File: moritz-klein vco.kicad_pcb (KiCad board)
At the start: 2 copper layers, 150 x 100 mm, 92 parts, among them J1 AudioJack2_SwitchT, J10 AudioJack2_SwitchT, J11 AudioJack2_SwitchT, J12 AudioJack2_SwitchT, J13 Conn_02x05_Odd_Even, J2 AudioJack2_SwitchT, J3 AudioJack2_SwitchT, J4 AudioJack2_SwitchT, J5 AudioJack2_SwitchT, J6 AudioJack2_SwitchT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

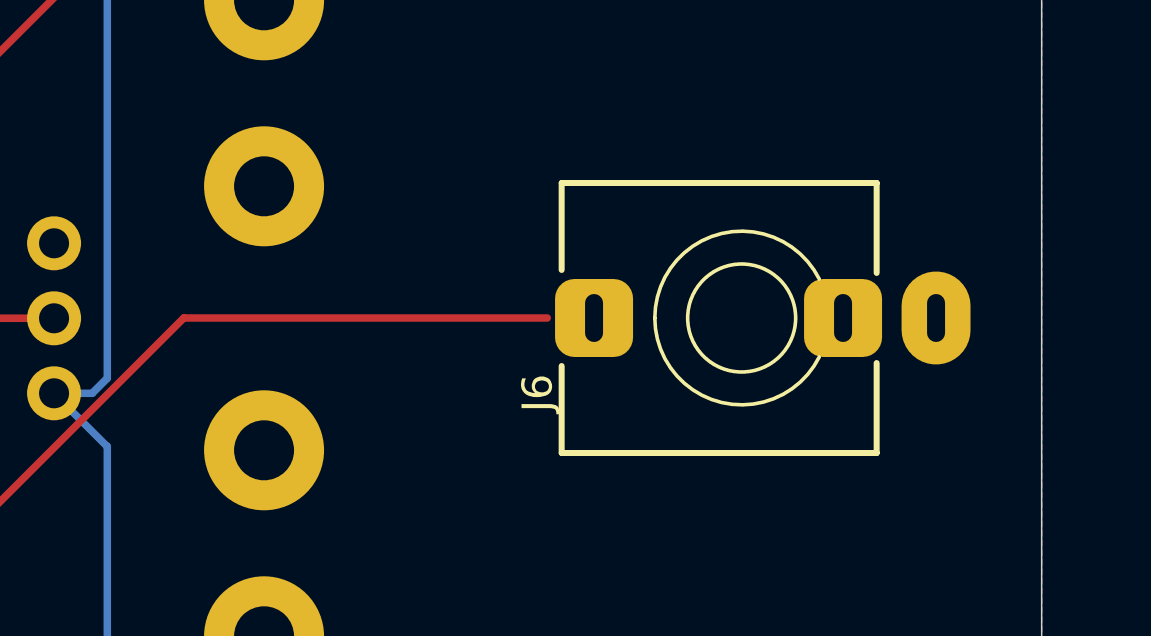
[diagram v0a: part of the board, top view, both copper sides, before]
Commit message: Jack was on the wrong side of the pcb.
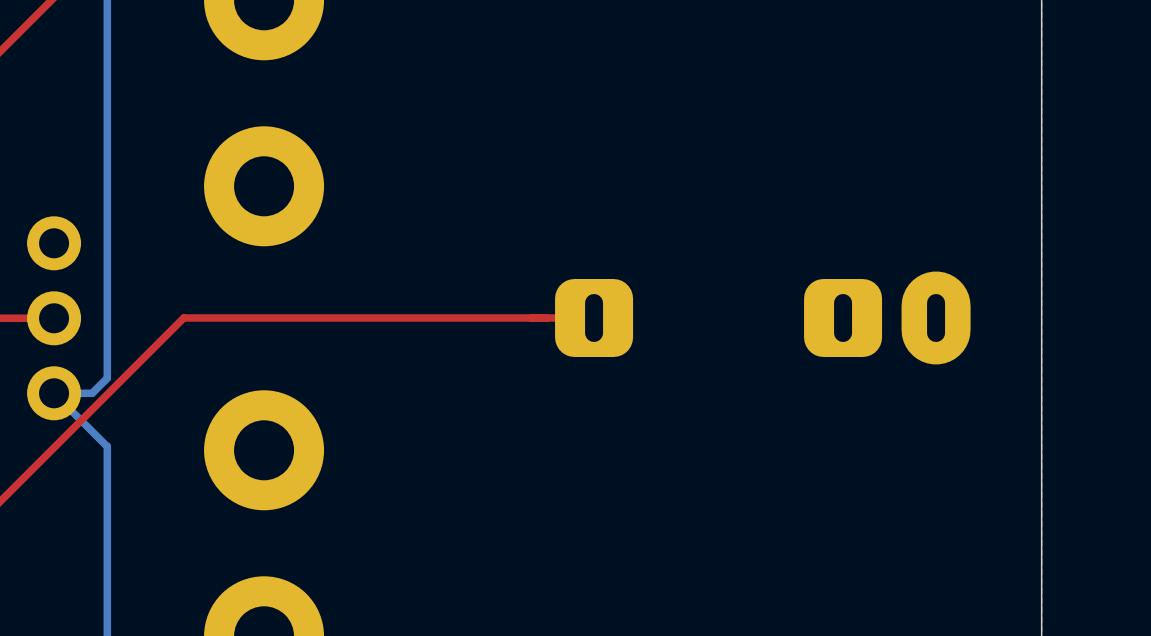
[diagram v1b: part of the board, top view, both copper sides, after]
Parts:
- J6: moved to B.Cu
- turned J6 to 270 degrees
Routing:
- net /cv_in_f: track 24.5 -> 26.6 mm
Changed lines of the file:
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@@
     (thickness 1.6)
     (drawings 12)
-    (tracks 315)
+    (tracks 317)
     (zones 0)
     (modules 92)
@@
     )
   )
-  (module AudioJacks:Jack_3.5mm_QingPu_WQP-PJ398SM_Vertical (layer F.Cu)
-    (at 220 82 90)
+  (module AudioJacks:Jack_3.5mm_QingPu_WQP-PJ398SM_Vertical (layer B.Cu)
+    (at 220 82 270)
     (descr "T-S-SN Vertical mount jack AKA WQP-WQP518MA or Thonkiconn")
     (tags "WQP-WQP518MA, Thonkiconn")
-    (fp_text reference J6 (at -2.5 -6.8 90) (layer F.SilkS)
-      (effects (font (size 1 1) (thickness 0.15)))
+    (fp_text reference J6 (at -2.5 6.8 270) (layer B.SilkS)
+      (effects (font (size 1 1) (thickness 0.15)) (justify mirror))
     )
-    (fp_text value AudioJack2_SwitchT (at 0 -5 90) (layer F.Fab)
-      (effects (font (size 1 1) (thickness 0.15)))
+    (fp_text value AudioJack2_SwitchT (at 0 5 270) (layer B.Fab)
+      (effects (font (size 1 1) (thickness 0.15)) (justify mirror))
     )
-    (fp_text user KEEPOUT (at 0 0 270) (layer Cmts.User)
+    (fp_text user KEEPOUT (at 0 0 90) (layer Cmts.User)
       (effects (font (size 0.4 0.4) (thickness 0.051)))
     )
-    (fp_text user %R (at 4.5 -9.5 90) (layer F.Fab)
-      (effects (font (size 1 1) (thickness 0.15)))
+    (fp_text user %R (at 4.5 9.5 270) (layer B.Fab)
+      (effects (font (size 1 1) (thickness 0.15)) (justify mirror))
     )
-    (fp_arc (start 0 0) (end 0 -2.895) (angle 153.4) (layer F.SilkS) (width 0.12))
-    (fp_arc (start 0 0) (end 0 -2.895) (angle -153.4) (layer F.SilkS) (width 0.12))
-    (fp_line (start 0 0) (end 0 -2.03) (layer F.Fab) (width 0.1))
-    (fp_circle (center 0 0.02) (end -1.8 0.02) (layer F.Fab) (width 0.1))
-    (fp_line (start -4.5 4.47) (end 4.5 4.47) (layer F.Fab) (width 0.1))
-    (fp_line (start -5 7.58) (end 5 7.58) (layer F.CrtYd) (width 0.05))
-    (fp_line (start -5 -7.25) (end 5 -7.25) (layer F.CrtYd) (width 0.05))
-    (fp_line (start -5 -7.25) (end -5 7.58) (layer F.CrtYd) (width 0.05))
-    (fp_line (start -4.5 -5.98) (end 4.5 -5.98) (layer F.Fab) (width 0.1))
-    (fp_line (start -4.5 -5.98) (end -4.5 4.42) (layer F.Fab) (width 0.1))
-    (fp_circle (center 0 0) (end -1.8 0) (layer F.SilkS) (width 0.12))
-    (fp_line (start 1.5 4.5) (end 4.5 4.5) (layer F.SilkS) (width 0.2))
-    (fp_line (start -4.5 4.5) (end -1.5 4.5) (layer F.SilkS) (width 0.2))
-    (fp_line (start 1.6 -6) (end 4.5 -6) (layer F.SilkS) (width 0.2))
-    (fp_line (start -4.5 -6) (end -1.6 -6) (layer F.SilkS) (width 0.2))
-    (fp_line (start 1.41 0.46) (end 0.46 1.41) (layer Dwgs.User) (width 0.12))
-    (fp_line (start 1.42 -0.395) (end -0.4 1.42) (layer Dwgs.User) (width 0.12))
-    (fp_line (start 1.07 -1.01) (end -1.01 1.07) (layer Dwgs.User) (width 0.12))
-    (fp_line (start 0.58 -1.35) (end -1.36 0.59) (layer Dwgs.User) (width 0.12))
-    (fp_line (start -0.09 -1.48) (end -1.48 -0.09) (layer Dwgs.User) (width 0.12))
+    (fp_arc (start 0 0) (end 0 2.895) (angle -153.4) (layer B.SilkS) (width 0.12))
+    (fp_arc (start 0 0) (end 0 2.895) (angle 153.4) (layer B.SilkS) (width 0.12))
+    (fp_line (start 0 0) (end 0 2.03) (layer B.Fab) (width 0.1))
+    (fp_circle (center 0 -0.02) (end -1.8 -0.02) (layer B.Fab) (width 0.1))
+    (fp_line (start -4.5 -4.47) (end 4.5 -4.47) (layer B.Fab) (width 0.1))
+    (fp_line (start -5 -7.58) (end 5 -7.58) (layer B.CrtYd) (width 0.05))
+    (fp_line (start -5 7.25) (end 5 7.25) (layer B.CrtYd) (width 0.05))
+    (fp_line (start -5 7.25) (end -5 -7.58) (layer B.CrtYd) (width 0.05))
+    (fp_line (start -4.5 5.98) (end 4.5 5.98) (layer B.Fab) (width 0.1))
+    (fp_line (start -4.5 5.98) (end -4.5 -4.42) (layer B.Fab) (width 0.1))
+    (fp_circle (center 0 0) (end -1.8 0) (layer B.SilkS) (width 0.12))
+    (fp_line (start 1.5 -4.5) (end 4.5 -4.5) (layer B.SilkS) (width 0.2))
+    (fp_line (start -4.5 -4.5) (end -1.5 -4.5) (layer B.SilkS) (width 0.2))
+    (fp_line (start 1.6 6) (end 4.5 6) (layer B.SilkS) (width 0.2))
+    (fp_line (start -4.5 6) (end -1.6 6) (layer B.SilkS) (width 0.2))
+    (fp_line (start 1.41 -0.46) (end 0.46 -1.41) (layer Dwgs.User) (width 0.12))
+    (fp_line (start 1.42 0.395) (end -0.4 -1.42) (layer Dwgs.User) (width 0.12))
+    (fp_line (start 1.07 1.01) (end -1.01 -1.07) (layer Dwgs.User) (width 0.12))
+    (fp_line (start 0.58 1.35) (end -1.36 -0.59) (layer Dwgs.User) (width 0.12))
+    (fp_line (start -0.09 1.48) (end -1.48 0.09) (layer Dwgs.User) (width 0.12))
     (fp_circle (center 0 0) (end -1.5 0) (layer Dwgs.User) (width 0.12))
-    (fp_line (start -4.5 4.5) (end -4.5 -6) (layer F.SilkS) (width 0.2))
-    (fp_line (start 4.5 4.5) (end 4.5 -6) (layer F.SilkS) (width 0.2))
-    (fp_line (start 4.5 -5.98) (end 4.5 4.42) (layer F.Fab) (width 0.1))
-    (fp_line (start 5 -7.25) (end 5 7.58) (layer F.CrtYd) (width 0.05))
-    (pad TN thru_hole roundrect (at 0 3.38 90) (size 2.6 2.6) (drill oval 1.6 0.6) (layers *.Cu *.Mask) (roundrect_rratio 0.25)
+    (fp_line (start -4.5 -4.5) (end -4.5 6) (layer B.SilkS) (width 0.2))
+    (fp_line (start 4.5 -4.5) (end 4.5 6) (layer B.SilkS) (width 0.2))
+    (fp_line (start 4.5 5.98) (end 4.5 -4.42) (layer B.Fab) (width 0.1))
+    (fp_line (start 5 7.25) (end 5 -7.58) (layer B.CrtYd) (width 0.05))
+    (pad TN thru_hole roundrect (at 0 -3.38 270) (size 2.6 2.6) (drill oval 1.6 0.6) (layers *.Cu *.Mask) (roundrect_rratio 0.25)
       (net 13 GND))
-    (pad S thru_hole oval (at 0 6.48 90) (size 3.1 2.3) (drill oval 1.6 0.6) (layers *.Cu *.Mask)
+    (pad S thru_hole oval (at 0 -6.48 270) (size 3.1 2.3) (drill oval 1.6 0.6) (layers *.Cu *.Mask)
       (net 13 GND))
-    (pad T thru_hole roundrect (at 0 -4.92 90) (size 2.6 2.6) (drill oval 1.6 0.6) (layers *.Cu *.Mask) (roundrect_rratio 0.25)
+    (pad T thru_hole roundrect (at 0 4.92 270) (size 2.6 2.6) (drill oval 1.6 0.6) (layers *.Cu *.Mask) (roundrect_rratio 0.25)
       (net 56 /cv_in_f))
     (model ${KISYS3DMOD}/AudioJacks.3dshapes/PJ398SM.step
@@
   (segment (start 193.893002 89.51) (end 192.16 89.51) (width 0.25) (layer F.Cu) (net 56))
   (segment (start 201.403002 82) (end 193.893002 89.51) (width 0.25) (layer F.Cu) (net 56))
-  (segment (start 213.52 82) (end 201.403002 82) (width 0.25) (layer F.Cu) (net 56))
+  (segment (start 215.08 82) (end 213 82) (width 0.25) (layer F.Cu) (net 56))
+  (segment (start 213 82) (end 201.403002 82) (width 0.25) (layer F.Cu) (net 56))
+  (segment (start 213.52 82) (end 213 82) (width 0.25) (layer F.Cu) (net 56))
   (zone (net 13) (net_name GND) (layer F.Cu) (hatch edge 0.508)
     (connect_pads (clearance 0.508))
